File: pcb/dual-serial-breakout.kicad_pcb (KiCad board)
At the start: 2 copper layers, 36 x 36 mm, 16 parts, among them P1 CONN_01X08

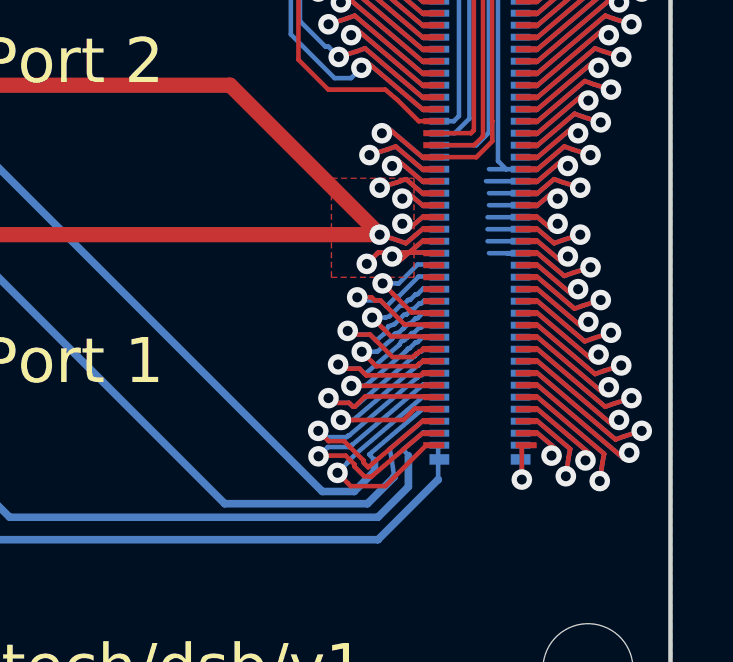
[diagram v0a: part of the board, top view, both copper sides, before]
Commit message: Fix up dual serial breakout DRC.
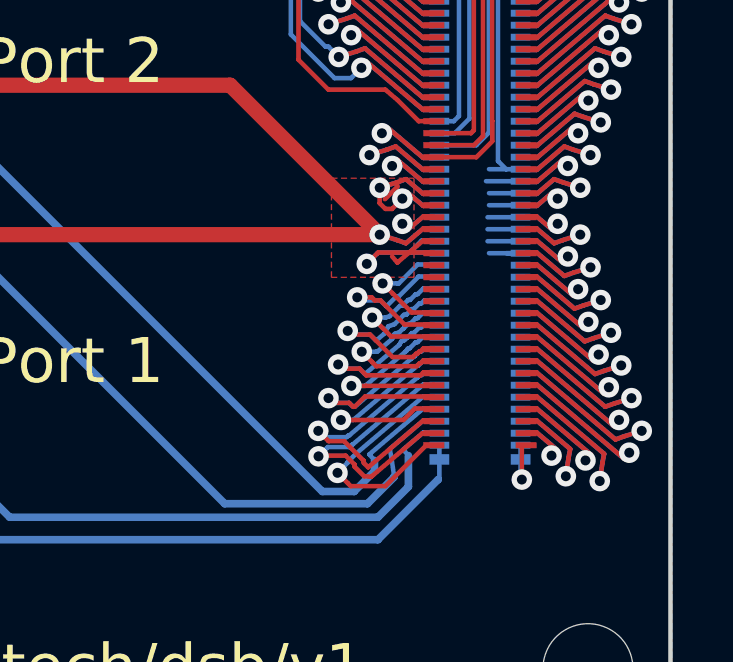
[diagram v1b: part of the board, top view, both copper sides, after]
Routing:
- net +5V: track 69.5 -> 71.4 mm, vias 6 -> 5
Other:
- net class Default: clearance 0.1524 -> 0.14986
- rule trace_clearance: 0.1524 -> 0.14986
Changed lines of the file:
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@@
 (kicad_pcb (version 4) (host pcbnew "(2015-11-03 BZR 6296)-product")
   (general
-    (links 0)
-    (no_connects 18)
+    (links 127)
+    (no_connects 1)
     (area 129.924999 89.924999 166.075001 126.075001)
     (thickness 1.6)
     (drawings 73)
-    (tracks 947)
+    (tracks 958)
     (zones 0)
     (modules 16)
@@
     (40 Dwgs.User user)
     (41 Cmts.User user)
-    (42 Eco1.User user hide)
-    (43 Eco2.User user hide)
+    (42 Eco1.User user)
+    (43 Eco2.User user)
     (44 Edge.Cuts user)
     (45 Margin user)
@@
     (user_trace_width 0.254)
     (user_trace_width 0.508)
-    (trace_clearance 0.1524)
+    (trace_clearance 0.14986)
     (zone_clearance 0.508)
     (zone_45_only no)
@@
     (visible_elements FFFFFF7F)
     (pcbplotparams
-      (layerselection 0x00030_80000001)
-      (usegerberextensions false)
+      (layerselection 0x010f0_80000001)
+      (usegerberextensions true)
       (excludeedgelayer true)
       (linewidth 0.100000)
@@
       (outputformat 1)
       (mirror false)
-      (drillshape 1)
+      (drillshape 0)
       (scaleselection 1)
-      (outputdirectory ""))
+      (outputdirectory gerber/))
   )
   (net 0 "")
@@
   (net 76 "Net-(PORT_OUT1-Pad25)")
   (net_class Default "This is the default net class."
-    (clearance 0.1524)
+    (clearance 0.14986)
     (trace_width 0.1524)
     (via_dia 0.6858)
@@
   (segment (start 154.733499 98.433499) (end 154.733499 95.812323) (width 0.1524) (layer F.Cu) (net 11))
   (segment (start 154.733499 95.812323) (end 155.146302 95.39952) (width 0.1524) (layer F.Cu) (net 11))
+  (segment (start 161.005 116.2) (end 161.005 116.905486) (width 0.1524) (layer B.Cu) (net 12))
+  (segment (start 161.005 116.905486) (end 161.045015 116.945501) (width 0.1524) (layer B.Cu) (net 12))
+  (segment (start 161.005 115.8) (end 161.005 116.2) (width 0.1524) (layer B.Cu) (net 12))
   (via (at 161.045015 116.945501) (size 0.685801) (drill 0.330201) (layers F.Cu B.Cu) (net 12))
-  (segment (start 161.045015 115.8002) (end 161.045015 116.945501) (width 0.1524) (layer B.Cu) (net 12))
   (segment (start 161.045015 115.8002) (end 161.045015 116.945501) (width 0.1524) (layer F.Cu) (net 12))
+  (segment (start 158.295 116.2) (end 158.295 116.906118) (width 0.1524) (layer B.Cu) (net 13))
+  (segment (start 158.295 116.906118) (end 158.255617 116.945501) (width 0.1524) (layer B.Cu) (net 13))
+  (segment (start 158.295 115.8) (end 158.295 116.2) (width 0.1524) (layer B.Cu) (net 13))
   (segment (start 156.25 118.95) (end 142.1824 118.95) (width 0.254) (layer B.Cu) (net 13))
   (segment (start 142.1824 118.95) (end 134.6524 111.42) (width 0.254) (layer B.Cu) (net 13))
@@
   (segment (start 158.254499 116.945501) (end 156.25 118.95) (width 0.254) (layer B.Cu) (net 13))
   (segment (start 158.255617 116.945501) (end 158.254499 116.945501) (width 0.254) (layer B.Cu) (net 13))
-  (segment (start 158.255617 115.8002) (end 158.255617 116.945501) (width 0.1524) (layer B.Cu) (net 13))
   (segment (start 161.005 99.8) (end 161.005 100.2) (width 0.1524) (layer B.Cu) (net 14))
   (segment (start 161.045015 99.054899) (end 161.045015 99.759985) (width 0.1524) (layer B.Cu) (net 14))
@@
   (segment (start 157.760316 107.024) (end 156.894127 106.287883) (width 0.1524) (layer F.Cu) (net 56))
   (segment (start 156.894127 106.287883) (end 156.721418 106.491109) (width 0.1524) (layer F.Cu) (net 56))
+  (segment (start 156.892034 107.187966) (end 156.48 107.6) (width 0.1524) (layer F.Cu) (net 57))
+  (segment (start 156.892034 107.036104) (end 156.892034 107.187966) (width 0.1524) (layer F.Cu) (net 57))
+  (segment (start 156.496001 107.923999) (end 156.306694 107.734692) (width 0.1524) (layer F.Cu) (net 57))
+  (segment (start 156.306694 107.734692) (end 156.306694 107.218712) (width 0.1524) (layer F.Cu) (net 57))
+  (segment (start 157.06265 107.5811) (end 156.719751 107.923999) (width 0.1524) (layer F.Cu) (net 57))
+  (segment (start 156.719751 107.923999) (end 156.496001 107.923999) (width 0.1524) (layer F.Cu) (net 57))
+  (segment (start 157.760316 107.824) (end 157.784316 107.8) (width 0.1524) (layer B.Cu) (net 57))
+  (segment (start 157.784316 107.8) (end 158.295 107.8) (width 0.1524) (layer B.Cu) (net 57))
+  (segment (start 157.760316 107.424) (end 157.784316 107.4) (width 0.1524) (layer B.Cu) (net 57))
+  (segment (start 157.784316 107.4) (end 158.295 107.4) (width 0.1524) (layer B.Cu) (net 57))
+  (segment (start 158.110316 109.376401) (end 157.31 109.376401) (width 0.1524) (layer B.Cu) (net 57))
+  (segment (start 157.31 109.376401) (end 156.256233 109.376401) (width 0.1524) (layer B.Cu) (net 57))
+  (segment (start 158.110316 108.976401) (end 157.71 108.976401) (width 0.1524) (layer B.Cu) (net 57))
+  (segment (start 157.71 108.976401) (end 157.31 109.376401) (width 0.1524) (layer B.Cu) (net 57))
   (segment (start 156.306694 108.781689) (end 139.678311 108.781689) (width 0.508) (layer F.Cu) (net 57))
   (segment (start 139.678311 108.781689) (end 136.024 112.436) (width 0.508) (layer F.Cu) (net 57))
@@
   (segment (start 156.220087 109.412547) (end 155.877188 109.755446) (width 0.1524) (layer B.Cu) (net 57))
   (segment (start 156.220087 109.412547) (end 155.877188 109.755446) (width 0.1524) (layer F.Cu) (net 57))
-  (segment (start 158.110316 109.376401) (end 156.256233 109.376401) (width 0.1524) (layer B.Cu) (net 57))
   (via (at 156.306694 107.218712) (size 0.685801) (drill 0.330201) (layers F.Cu B.Cu) (net 57))
-  (segment (start 158.110316 107.424) (end 157.760316 107.424) (width 0.1524) (layer B.Cu) (net 57))
   (segment (start 157.760316 107.424) (end 157.180872 106.931569) (width 0.1524) (layer B.Cu) (net 57))
   (segment (start 157.180872 106.931569) (end 156.892034 107.036104) (width 0.1524) (layer B.Cu) (net 57))
@@
   (segment (start 156.892034 107.036104) (end 156.306694 107.218712) (width 0.1524) (layer F.Cu) (net 57))
   (via (at 157.06265 107.5811) (size 0.685801) (drill 0.330201) (layers F.Cu B.Cu) (net 57))
-  (segment (start 158.110316 107.824) (end 157.760316 107.824) (width 0.1524) (layer B.Cu) (net 57))
   (segment (start 157.760316 107.824) (end 157.235359 107.377873) (width 0.1524) (layer B.Cu) (net 57))
   (segment (start 157.235359 107.377873) (end 157.06265 107.5811) (width 0.1524) (layer B.Cu) (net 57))
@@
   (segment (start 157.180872 109.068832) (end 156.892034 108.964297) (width 0.1524) (layer F.Cu) (net 57))
   (segment (start 156.892034 108.964297) (end 156.306694 108.781689) (width 0.1524) (layer F.Cu) (net 57))
-  (via (at 156.721418 109.509292) (size 0.685801) (drill 0.330201) (layers F.Cu B.Cu) (net 57))
-  (segment (start 158.110316 108.976401) (end 157.760316 108.976401) (width 0.1524) (layer B.Cu) (net 57))
-  (segment (start 157.760316 108.976401) (end 156.894127 109.712518) (width 0.1524) (layer B.Cu) (net 57))
-  (segment (start 156.894127 109.712518) (end 156.721418 109.509292) (width 0.1524) (layer B.Cu) (net 57))
   (segment (start 158.110316 108.976401) (end 157.760316 108.976401) (width 0.1524) (layer F.Cu) (net 57))
   (segment (start 157.760316 108.976401) (end 156.894127 109.712518) (width 0.1524) (layer F.Cu) (net 57))

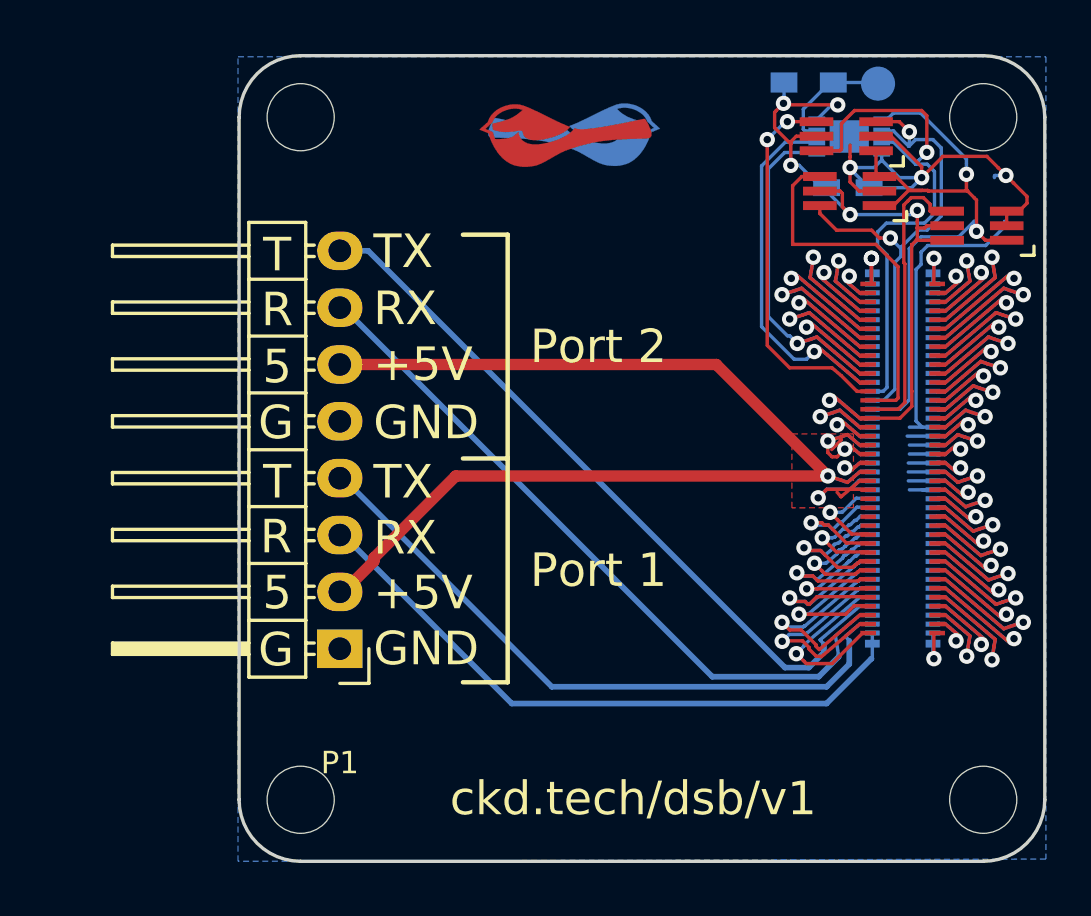
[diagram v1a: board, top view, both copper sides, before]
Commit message: Add logic level conversion.
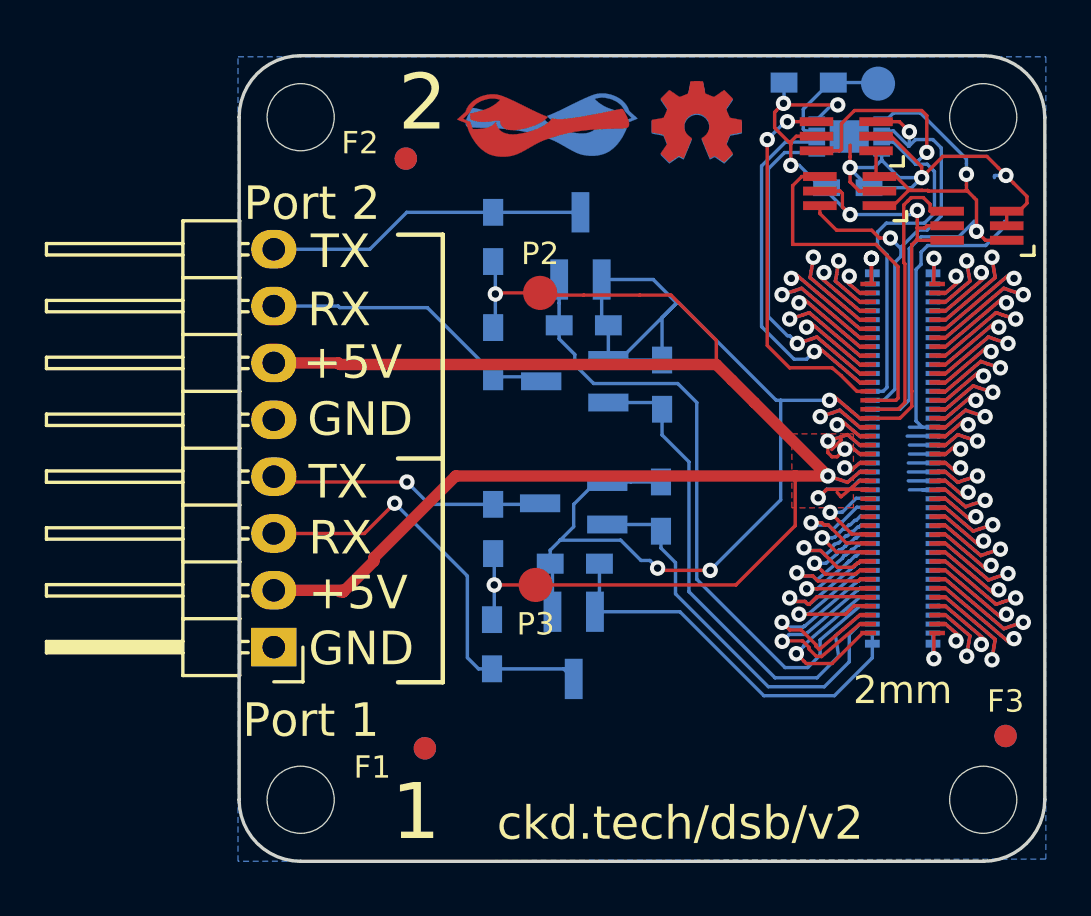
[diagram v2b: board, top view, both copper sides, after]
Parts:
- added F1: 1mm, macrofab:Fiducial, F.Cu at (138.3, 121.0)
- added F2: 1mm, macrofab:Fiducial, F.Cu at (137.4, 94.6)
- added F3: 1mm, macrofab:Fiducial, F.Cu at (164.2, 120.4)
- added F4: 1mm, macrofab:Fiducial, B.Cu at (138.3, 121.0)
- added F5: 1mm, macrofab:Fiducial, B.Cu at (137.4, 94.6)
- added F6: 1mm, macrofab:Fiducial, B.Cu at (164.2, 120.4)
- added G***: OSHW, oshw:oshw-4mm, B.Cu at (150.4, 93.0)
- added G***: OSHW, oshw:oshw-4mm, F.Cu at (150.4, 93.0)
- added P2: CONN_01X01, Measurement_Points:Measurement_Point_Round-SMD-Pad_Small, F.Cu at (143.4, 100.6)
- added P3: CONN_01X01, Measurement_Points:Measurement_Point_Round-SMD-Pad_Small, F.Cu at (143.2, 113.7)
- added Q1: BSS138, TO_SOT_Packages_SMD:SOT-23_Handsoldering, B.Cu at (145.2, 98.5)
- added Q2: BSS138, TO_SOT_Packages_SMD:SOT-23_Handsoldering, B.Cu at (145.0, 104.5)
- added Q3: BSS138, TO_SOT_Packages_SMD:SOT-23_Handsoldering, B.Cu at (144.9, 110.0)
- added Q4: BSS138, TO_SOT_Packages_SMD:SOT-23_Handsoldering, B.Cu at (144.9, 116.3)
- added R1: 10k, Resistors_SMD:R_0603_HandSoldering, B.Cu at (141.3, 98.1)
- added R2: 10k, Resistors_SMD:R_0603_HandSoldering, B.Cu at (141.3, 103.2)
- added R3: 10k, Resistors_SMD:R_0603_HandSoldering, B.Cu at (141.3, 111.2)
- added R4: 10k, Resistors_SMD:R_0603_HandSoldering, B.Cu at (141.3, 116.3)
- added R5: 10k, Resistors_SMD:R_0603_HandSoldering, B.Cu at (145.4, 102.0)
- added R6: 10k, Resistors_SMD:R_0603_HandSoldering, B.Cu at (148.9, 104.7)
- added R7: 10k, Resistors_SMD:R_0603_HandSoldering, B.Cu at (148.8, 110.2)
- added R8: 10k, Resistors_SMD:R_0603_HandSoldering, B.Cu at (145.0, 112.7)
- moved P1 2.95 mm to (131.6, 116.4)
- moved G*** 1.10 mm to (144.0, 93.1)
- moved G*** 1.10 mm to (143.6, 93.1)
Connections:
- net /ExpansionPort/3V3_0.3A_LL renamed +3V3
- P1 pad 3: /ExpansionPort/UART1_RX -> /RX1_HV1
- P1 pad 4: /ExpansionPort/UART1_TX -> /TX1_HV1
- P1 pad 7: /ExpansionPort/UART2_RX -> /RX2_HV2
- P1 pad 8: /ExpansionPort/UART2_TX -> /TX2_HV2
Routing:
- net +3V3: track 36.2 -> 87.4 mm, vias 6 -> 8
- net +5V: track 71.4 -> 112.1 mm, vias 5 -> 7
- net /RX1_HV1: track 0.00 -> 19.4 mm, vias 0 -> 1
- net /TX2_HV2: track 0.00 -> 14.4 mm
- net /RX2_HV2: track 0.00 -> 13.4 mm
- net /TX1_HV1: track 0.00 -> 12.4 mm, vias 0 -> 1
- net /ExpansionPort/UART1_TX: track 29.6 -> 17.8 mm
- net /ExpansionPort/UART1_RX: track 28.9 -> 18.0 mm
- net /ExpansionPort/UART2_RX: track 32.3 -> 22.6 mm
- net /ExpansionPort/UART2_TX: track 33.0 -> 28.9 mm
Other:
- board text added: "1"
- board text added: "2"
- board text added: "2mm"
- board text added: "ckd.tech/dsb/v2"
- board text removed: "5"
- board text removed: "G"
- board text removed: "R"
- board text removed: "T"
- board text removed: "ckd.tech/dsb/v1"

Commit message: Rebrand everything to Polystack and increment versions.
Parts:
- added svg2mod: G***, polystack:polystack-medium-0.4, B.Cu at (164.9, 107.9)
- added svg2mod: G***, polystack:polystack-medium-0.625, B.Cu at (153.2, 121.9)
- added svg2mod: G***, polystack:polystack-medium-0.625, F.Cu at (153.2, 121.9)
- added svg2mod: G***, polystack:polystack-medium-0.4, F.Cu at (164.9, 107.9)
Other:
- rule pad_to_mask_clearance: 0.2 -> 0.0762

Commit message: Final gerbers for test manufacturing run.
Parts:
- moved G*** 8.50 mm to (141.9, 93.0)
- moved G*** 4.75 mm to (148.3, 93.1)
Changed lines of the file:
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@@
 (kicad_pcb (version 4) (host pcbnew 4.0.1-stable)
   (general
-    (links 0)
-    (no_connects 1)
-    (area 129.924999 89.924999 166.075001 126.075001)
+    (links 153)
+    (no_connects 0)
+    (area 118.127143 74.1 269.404765 178)
     (thickness 1.6)
     (drawings 62)
@@
   )
   (module chickadee:chickadee_3mm_fcu (layer F.Cu)
-    (at 143.55 93.12)
+    (at 148.3 93.1)
     (fp_text reference G*** (at 0 0) (layer F.SilkS) hide
       (effects (font (thickness 0.3)))
@@
   )
   (module oshw:oshw-4mm (layer F.Cu)
-    (at 150.45 92.95)
+    (at 141.95 92.95)
     (fp_text reference G*** (at 0 0) (layer F.SilkS) hide
       (effects (font (thickness 0.3)))
@@
   (segment (start 157.760316 107.024) (end 156.894127 106.287883) (width 0.1524) (layer F.Cu) (net 55))
   (segment (start 156.894127 106.287883) (end 156.721418 106.491109) (width 0.1524) (layer F.Cu) (net 55))
+  (segment (start 158.11 109) (end 156.525005 109) (width 0.1524) (layer F.Cu) (net 56))
+  (segment (start 156.525005 109) (end 156.306694 108.781689) (width 0.1524) (layer F.Cu) (net 56))
+  (segment (start 158.11 109) (end 157.783915 109) (width 0.1524) (layer F.Cu) (net 56))
   (segment (start 134.5 103.8) (end 134.43 103.73) (width 0.508) (layer F.Cu) (net 56))
   (segment (start 134.43 103.73) (end 131.55 103.73) (width 0.508) (layer F.Cu) (net 56))
@@
   (segment (start 157.180872 109.068832) (end 156.892034 108.964297) (width 0.1524) (layer F.Cu) (net 56))
   (segment (start 156.892034 108.964297) (end 156.306694 108.781689) (width 0.1524) (layer F.Cu) (net 56))
-  (segment (start 158.110316 108.976401) (end 157.760316 108.976401) (width 0.1524) (layer F.Cu) (net 56))
-  (segment (start 157.760316 108.976401) (end 156.894127 109.712518) (width 0.1524) (layer F.Cu) (net 56))
-  (segment (start 156.894127 109.712518) (end 156.721418 109.509292) (width 0.1524) (layer F.Cu) (net 56))
   (segment (start 156.889988 110.406564) (end 156.405055 110.406564) (width 0.1524) (layer B.Cu) (net 57))
   (segment (start 158.110316 111.376401) (end 157.374892 111.376401) (width 0.1524) (layer F.Cu) (net 57))
